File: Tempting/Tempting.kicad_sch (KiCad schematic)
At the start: 32 parts, among them J101 Conn_Coaxial, J102 Conn_ARM_SWD_TagConnect_TC2030, J103 USB_C_Receptacle_USB2.0_16P, U101 STM32WB55CGUx, U102 SCD41-D-R2, U103 USBLC6-2SC6, U104 AMS1117-3.3, X101 32M, X102 32.768k

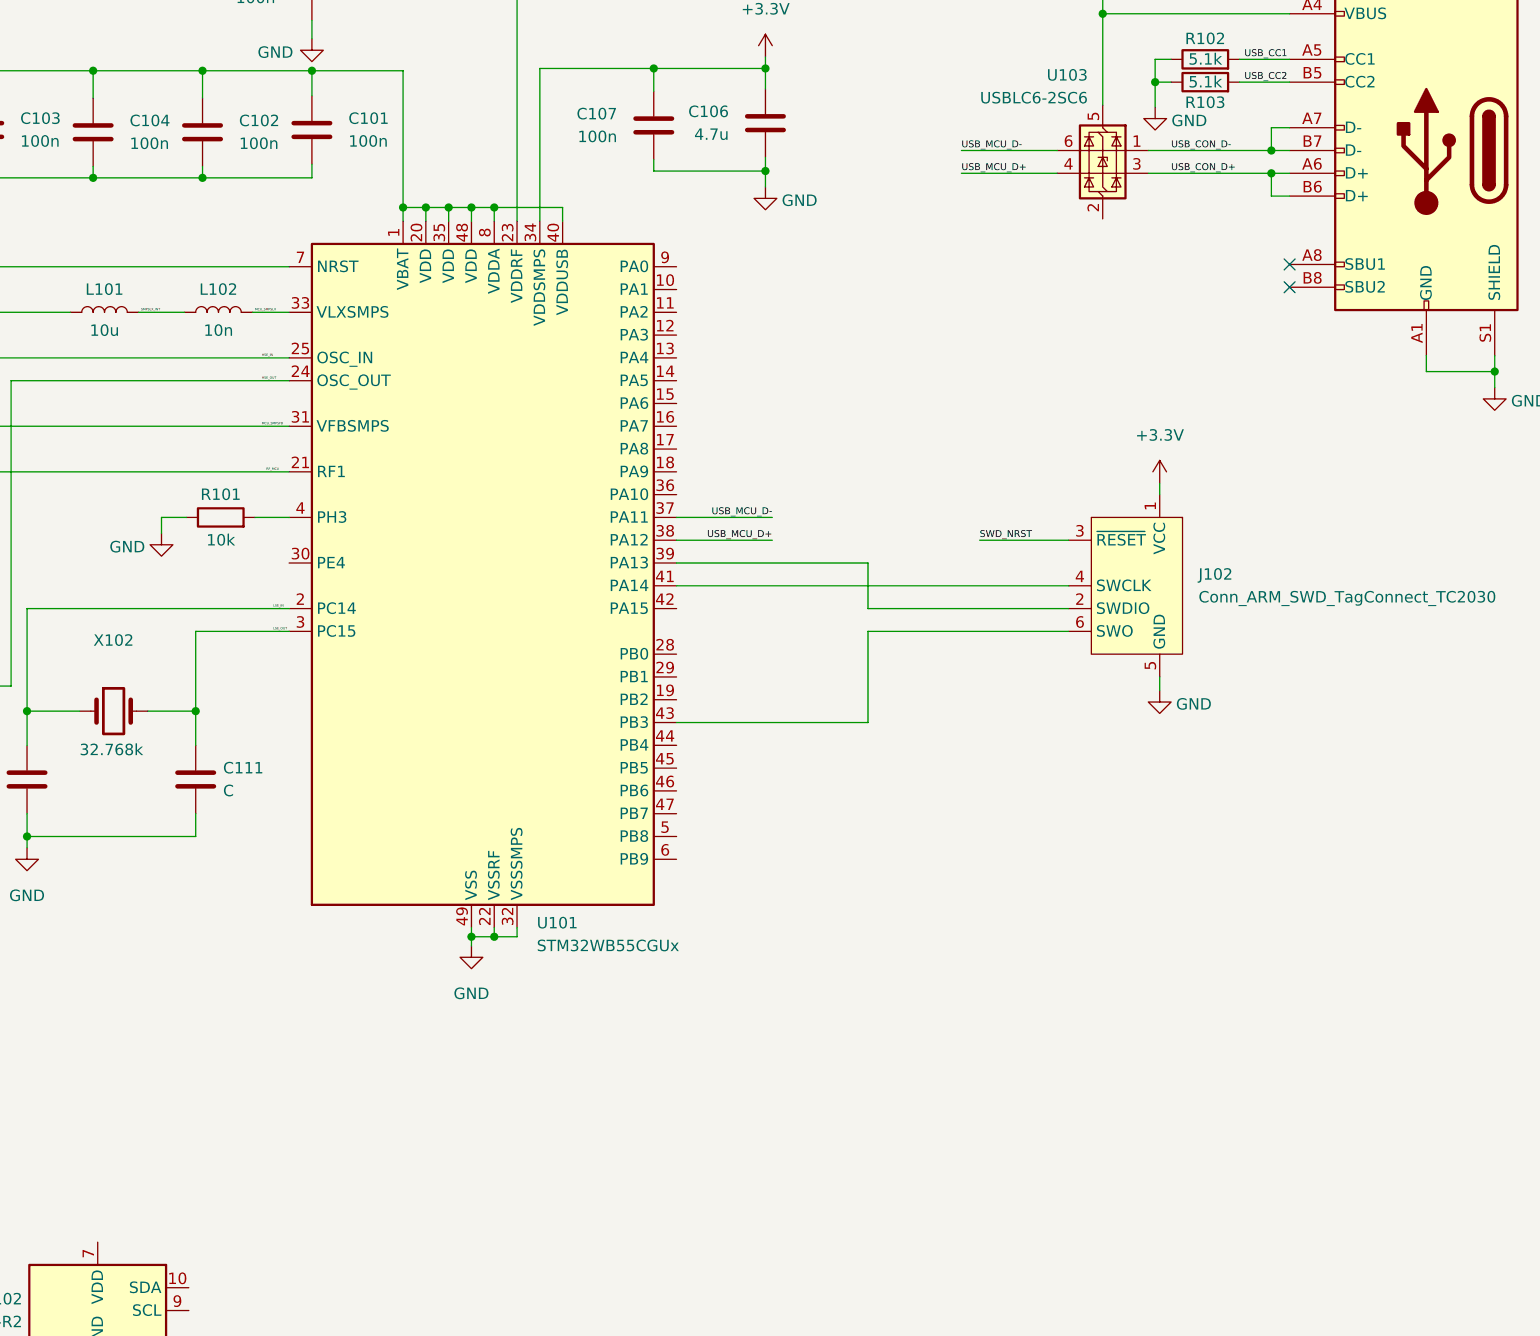
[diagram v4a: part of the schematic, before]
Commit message: Added OLED comm pins
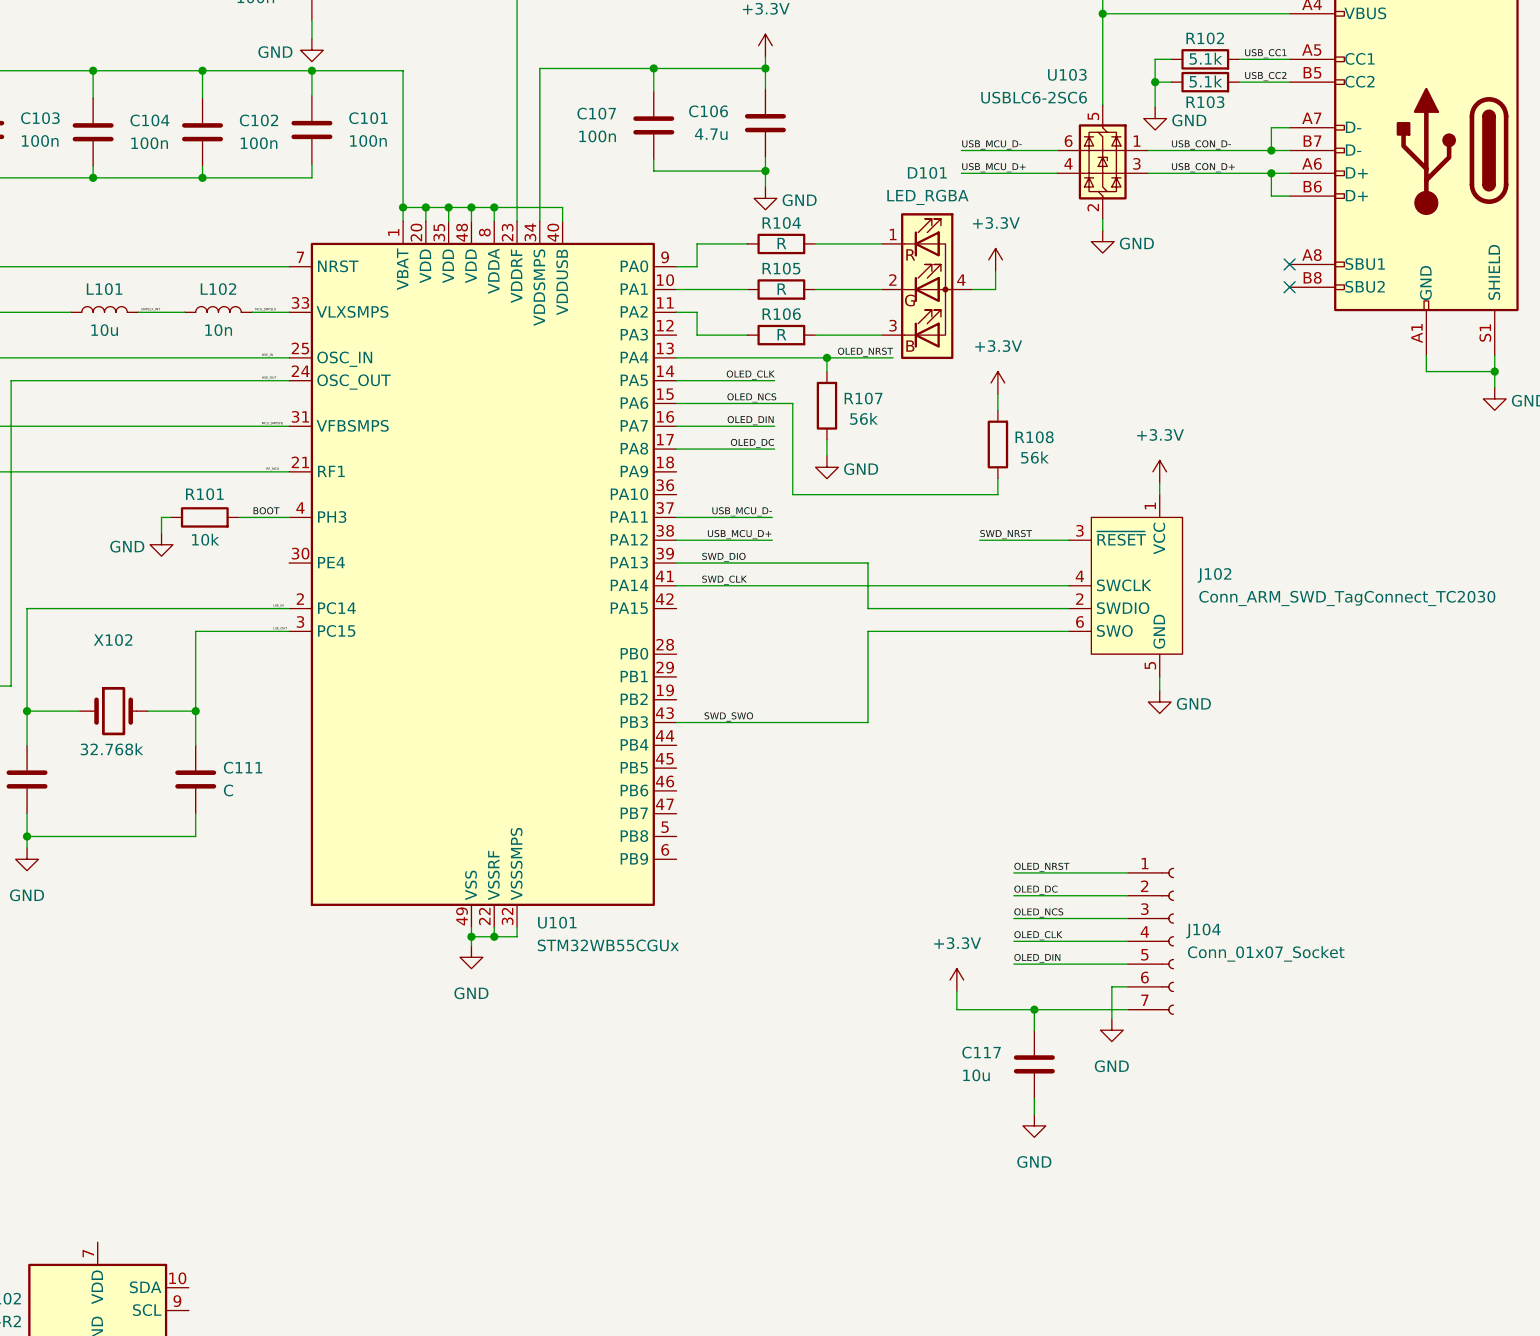
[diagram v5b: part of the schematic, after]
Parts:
- added C117: 10u, symbol Device:C
- added D101: LED_RGBA, symbol Device:LED_RGBA
- added J104: Conn_01x07_Socket, symbol Connector:Conn_01x07_Socket
- added R104, R105, R106: R, symbol Device:R
- added R107, R108: 56k, symbol Device:R
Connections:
- net +3.3V: now also C117.1, D101.4 (A), J104.7 (Pin_7), R108.2
- net GND: now also U103.2 (GND), C117.2, J104.6 (Pin_6), R107.1
- net at U101.10 (PA1): now also R105.1
- net at U101.11 (PA2): now also R106.1
- net OLED_NRST: now reaches U101.13 (PA4)
- net OLED_NRST: now also J104.1 (Pin_1), R107.2
- net OLED_CLK: now reaches U101.14 (PA5)
- net OLED_CLK: now also J104.4 (Pin_4)
- net OLED_NCS: now reaches U101.15 (PA6)
- net OLED_NCS: now also J104.3 (Pin_3), R108.1
- net OLED_DIN: now reaches U101.16 (PA7)
- net OLED_DIN: now also J104.5 (Pin_5)
- net OLED_DC: now reaches U101.17 (PA8)
- net OLED_DC: now also J104.2 (Pin_2)
- net SWD_DIO: now reaches J102.2 (SWDIO), U101.39 (PA13)
- net BOOT: now reaches R101.2, U101.4 (PH3)
- net SWD_CLK: now reaches J102.4 (SWCLK), U101.41 (PA14)
- net SWD_SWO: now reaches J102.6 (SWO), U101.43 (PB3)
- net at U101.9 (PA0): now also R104.1
- new net: D101.1 (RK), R104.2
- new net: D101.2 (GK), R105.2
- new net: D101.3 (BK), R106.2
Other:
- moved on the sheet: R101

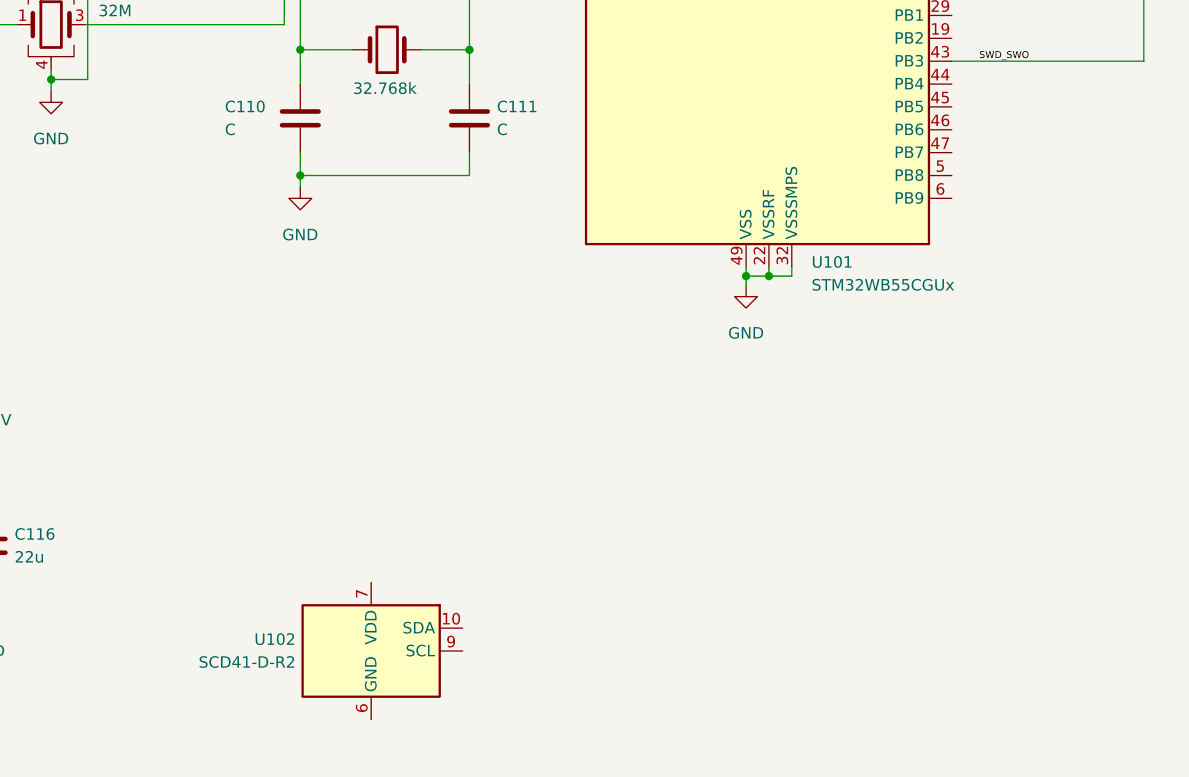
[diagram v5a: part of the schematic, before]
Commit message: Added circuitry for SCD41
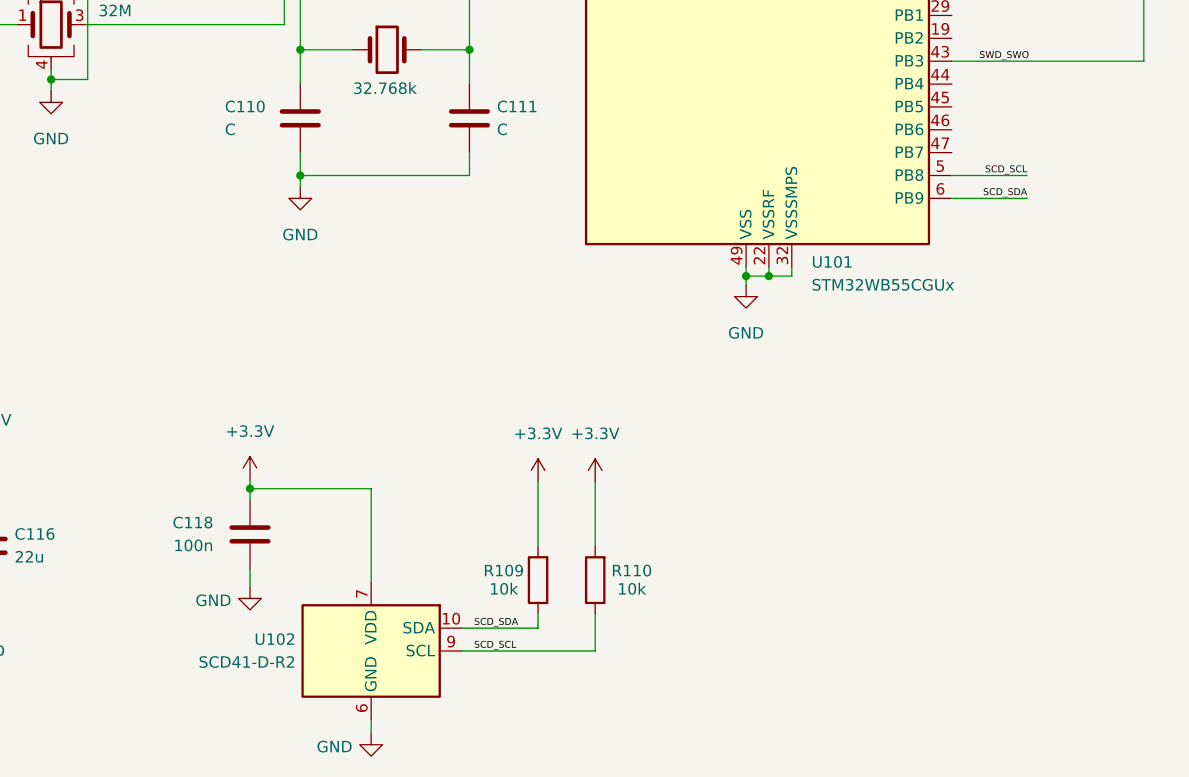
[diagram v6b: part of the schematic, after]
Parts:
- added C118: 100n, symbol Device:C
- added R109, R110: 10k, symbol Device:R
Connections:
- net +3.3V: now also U102.19 (VDD), U102.7 (VDD), C118.1, R109.2, R110.2
- net GND: now also U102.20 (GND), U102.21 (GND), U102.6 (GND), C118.2
- net SCD_SDA: now reaches U102.10 (SDA)
- net SCD_SDA: now also U101.6 (PB9), R109.1
- net SCD_SCL: now reaches U102.9 (SCL)
- net SCD_SCL: now also U101.5 (PB8), R110.1

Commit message: Cleaned up and finished schematic
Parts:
- added C119, C120, C121, C122: 100n, symbol Device:C
- added SW101, SW102: SW_Push, symbol Switch:SW_Push
- added U105: DPS368, Tempting_Footprint_Libraries:DPS368, symbol Tempting_Symbol_Libraries:DPS368
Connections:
- net +3.3V: now also C119.1, C120.1, U105.6 (VDDIO), U105.8 (VDD)
- net GND: now also C119.2, C120.2, C121.2, C122.2, SW101.1, SW102.1, U105.1 (GND), U105.7 (GND)
- net BUTTON_1: now reaches U101.28 (PB0)
- net BUTTON_1: now also C121.1, SW101.2
- net BUTTON_2: now reaches U101.29 (PB1)
- net BUTTON_2: now also C122.1, SW102.2
- net SCD_SCL renamed SENSORS_SCL
- net SENSORS_SCL: now also R109.1, U105.4 (SCK); no longer R110.1
- net SCD_SDA renamed SENSORS_SDA
- net SENSORS_SDA: now also R110.1, U105.3 (SDI); no longer R109.1
- no-connect marks 2 -> 14
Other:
- note added: "MCU"
- note added: "OLED + Button Control"
- note added: "Power"
- note added: "Sensors"
- note added: "Tempting Services"
- note added: "USB + SWD"
- moved on the sheet: C101, C102, C103, C104, C105, C106, C107, C108, C109, C110, C111, C112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

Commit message: Added new footprints and assigned all footprints
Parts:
- removed SW101, SW102: SW_Push, symbol Switch:SW_Push
- added SW1, SW2: SPST, Tempting_Footprint_Libraries:2-1825910-7, symbol Switch:SW_MEC_5E
- C1: renamed from C115; footprint (none) -> Capacitor_SMD:C_0805_2012Metric
- C10: renamed from C104; footprint (none) -> Capacitor_SMD:C_0402_1005Metric
- C11: renamed from C111; footprint (none) -> Capacitor_SMD:C_0402_1005Metric
- C12: renamed from C102; footprint (none) -> Capacitor_SMD:C_0402_1005Metric
- C13: renamed from C118; footprint (none) -> Capacitor_SMD:C_0402_1005Metric
- C14: renamed from C108; footprint (none) -> Capacitor_SMD:C_0402_1005Metric
- C15: renamed from C101; footprint (none) -> Capacitor_SMD:C_0402_1005Metric
- C16: renamed from C107; footprint (none) -> Capacitor_SMD:C_0402_1005Metric
- C17: renamed from C106; footprint (none) -> Capacitor_SMD:C_0603_1608Metric
- C18: renamed from C120; footprint (none) -> Capacitor_SMD:C_0402_1005Metric
- C19: renamed from C119; footprint (none) -> Capacitor_SMD:C_0402_1005Metric
- C2: renamed from C116; footprint (none) -> Capacitor_SMD:C_0805_2012Metric
- C20: renamed from C117; footprint (none) -> Capacitor_SMD:C_0805_2012Metric
- C21: renamed from C121; footprint (none) -> Capacitor_SMD:C_0402_1005Metric
- C22: renamed from C122; footprint (none) -> Capacitor_SMD:C_0402_1005Metric
- C3: renamed from C113; footprint (none) -> Capacitor_SMD:C_0402_1005Metric
- C4: renamed from C114; footprint (none) -> Capacitor_SMD:C_0402_1005Metric
- C5: renamed from C105; footprint (none) -> Capacitor_SMD:C_0603_1608Metric
- C6: renamed from C112; footprint (none) -> Capacitor_SMD:C_0402_1005Metric
- C7: renamed from C109; footprint (none) -> Capacitor_SMD:C_0603_1608Metric
- C8: renamed from C103; footprint (none) -> Capacitor_SMD:C_0402_1005Metric
- C9: renamed from C110; footprint (none) -> Capacitor_SMD:C_0402_1005Metric
- D1: renamed from D101; footprint (none) -> Tempting_Footprint_Libraries:AAA3528LSEEZGKQBKS
- J1: renamed from J101; footprint (none) -> Connector_Coaxial:U.FL_Hirose_U.FL-R-SMT-1_Vertical
- J2: renamed from J104; footprint (none) -> Connector_PinSocket_2.54mm:PinSocket_1x07_P2.54mm_Vertical
- J4: renamed from J103; footprint (none) -> Connector_USB:USB_C_Receptacle_HRO_TYPE-C-31-M-12
- L1: renamed from L103; footprint (none) -> Inductor_SMD:L_0402_1005Metric
- L2: renamed from L101; footprint (none) -> Inductor_SMD:L_0805_2012Metric
- L3: renamed from L102; footprint (none) -> Inductor_SMD:L_0402_1005Metric
- R1: renamed from R101; footprint (none) -> Resistor_SMD:R_0402_1005Metric
- R10: renamed from R103; footprint (none) -> Resistor_SMD:R_0402_1005Metric
- R2: renamed from R104; value R -> 750R; footprint (none) -> Resistor_SMD:R_0402_1005Metric
- R3: renamed from R105; value R -> 500R; footprint (none) -> Resistor_SMD:R_0402_1005Metric
- R4: renamed from R106; value R -> 500R; footprint (none) -> Resistor_SMD:R_0402_1005Metric
- R5: renamed from R107; footprint (none) -> Resistor_SMD:R_0402_1005Metric
- R6: renamed from R109; footprint (none) -> Resistor_SMD:R_0402_1005Metric
- R7: renamed from R110; footprint (none) -> Resistor_SMD:R_0402_1005Metric
- R8: renamed from R108; footprint (none) -> Resistor_SMD:R_0402_1005Metric
- R9: renamed from R102; footprint (none) -> Resistor_SMD:R_0402_1005Metric
- X1: renamed from X101; footprint (none) -> Crystal:Crystal_SMD_2016-4Pin_2.0x1.6mm
- X2: renamed from X102; footprint (none) -> Crystal:Crystal_SMD_2012-2Pin_2.0x1.2mm
- renumbered FLT101 to FLT1, J102 to J3, U104 to U1, U102 to U2, U101 to U3, U105 to U4, U103 to U5
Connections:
- net +3.3V: now also D1.2 (A); no longer D1.4 (A)
- net BUTTON_1: now also SW1.4 (A)
- net BUTTON_2: now also SW2.4 (A)
- net GND: now also SW1.1, SW2.1
- net at R3.2: now also D1.3 (GK); no longer D1.2 (GK)
- net at R4.2: now also D1.4 (BK); no longer D1.3 (BK)
- no-connect marks 14 -> 18
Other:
- moved on the sheet: C21, C22
